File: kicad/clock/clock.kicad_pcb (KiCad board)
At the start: 2 copper layers, 48.9 x 36.2 mm, 22 parts, among them J1 HLT IN, J2 CLK OUT, J3 5V IN, J4 OSC A, J5 OSC B, SW1 SEL, U1 74LS04, U2 74LS08, U3 74LS32, U4 LM555

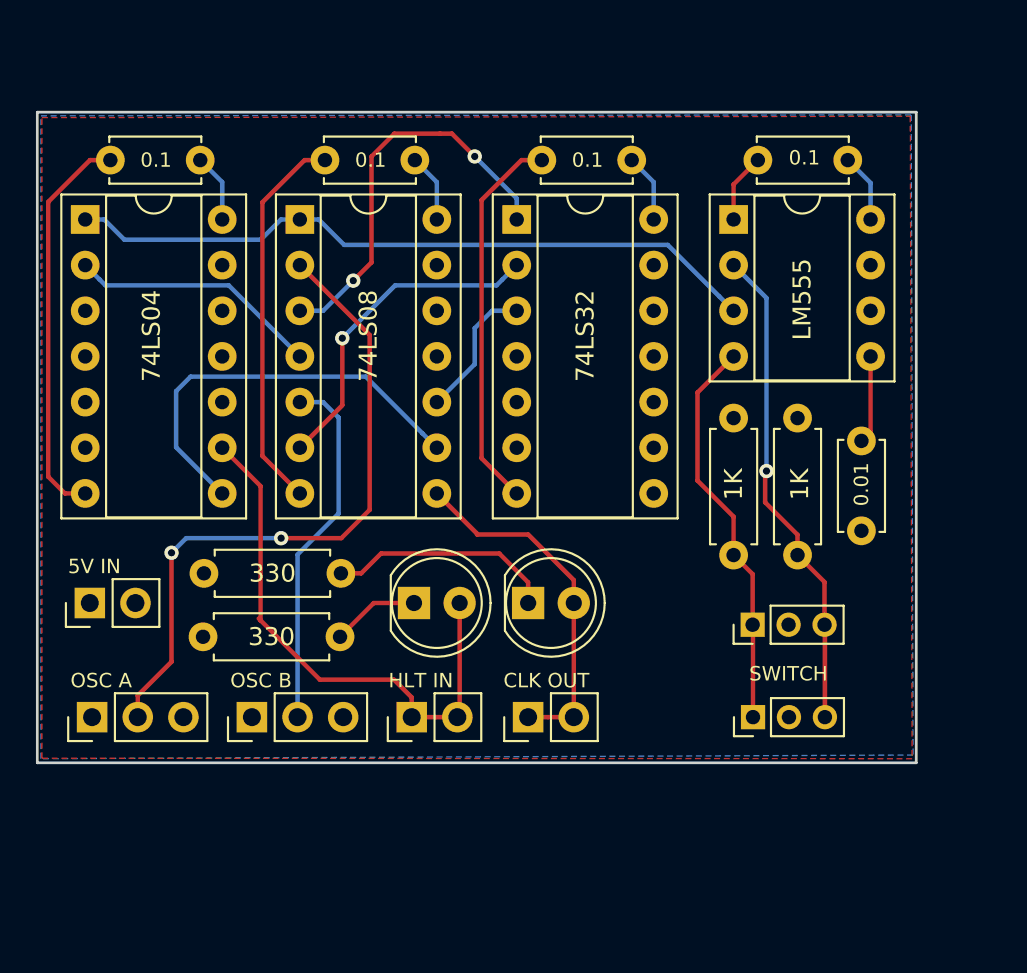
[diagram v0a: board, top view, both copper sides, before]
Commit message: More info on clock, plus gerbers
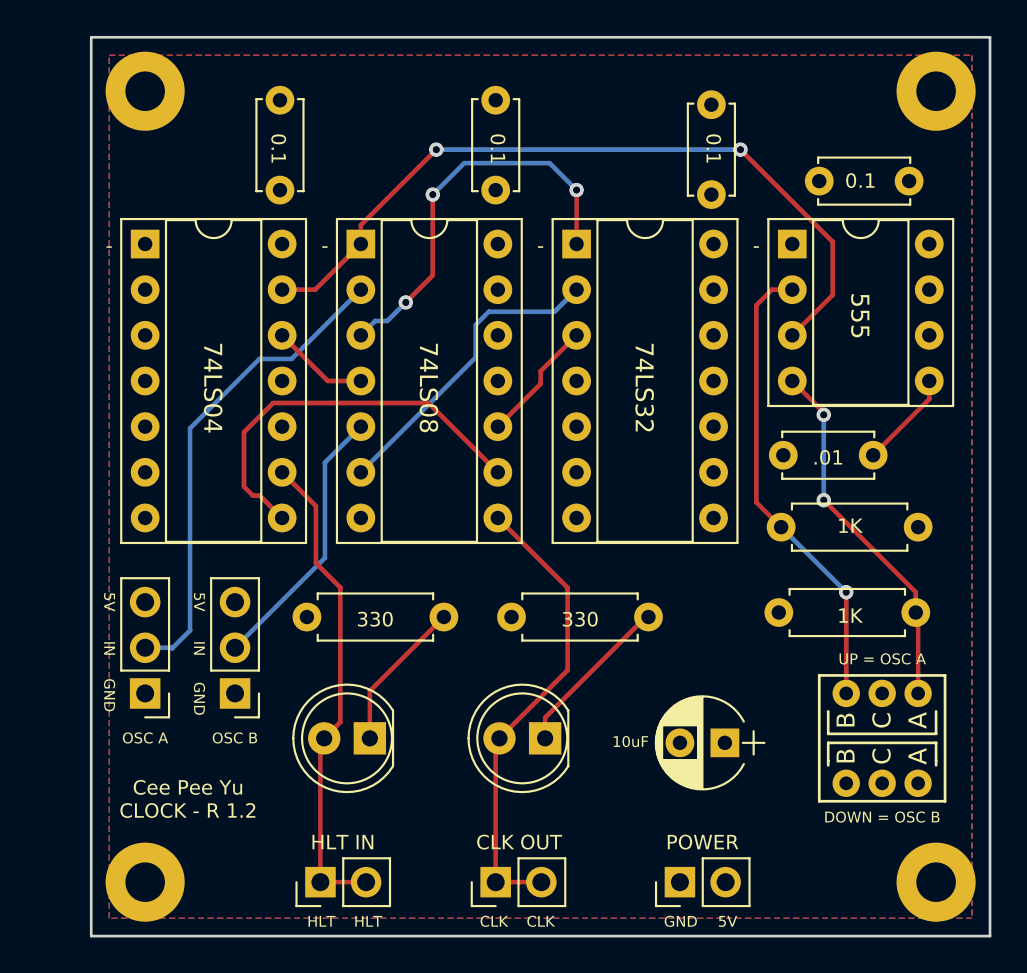
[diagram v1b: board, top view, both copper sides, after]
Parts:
- removed SWITCH: SEL, Socket_Strips:Socket_Strip_Straight_1x03_Pitch2.00mm
- added C6: 0.1uF, Capacitors_THT:C_Disc_D5.0mm_W2.5mm_P5.00mm, F.Cu at (164.5, 54.8)
- added REF**: MountingHole_2.2mm_M2_Pad, Mounting_Holes:MountingHole_2.2mm_M2_Pad, F.Cu at (177.0, 93.0)
- added REF**: MountingHole_2.2mm_M2_Pad, Mounting_Holes:MountingHole_2.2mm_M2_Pad, F.Cu at (133.0, 93.0)
- added REF**: MountingHole_2.2mm_M2_Pad, Mounting_Holes:MountingHole_2.2mm_M2_Pad, F.Cu at (177.0, 49.0)
- added REF**: MountingHole_2.2mm_M2_Pad, Mounting_Holes:MountingHole_2.2mm_M2_Pad, F.Cu at (133.0, 49.0)
- C1, C2, C3: value 0.1 -> 0.1uF
- C4: value 0.01 -> 0.01uF
- C5: value 0.1 -> 10uF; footprint Capacitors_THT:C_Disc_D5.0mm_W2.5mm_P5.00mm -> Capacitors_THT:CP_Radial_D5.0mm_P2.50mm
- J3: value 5V IN -> 5v IN
- SW1: value SEL -> SEL SW; footprint Socket_Strips:Socket_Strip_Straight_1x03_Pitch2.00mm -> Custom_Parts:SW_DPDT_L7mm_P2mm
- moved J3 36.3 mm to (162.8, 93.0)
- moved C5 33.1 mm to (165.2, 85.2)
- moved R2 17.3 mm to (161.0, 78.2)
- moved C3 15.5 mm to (170.5, 54.0)
- moved R4 11.1 mm to (168.2, 78.0), turned to 0 degrees
- moved J1 10.5 mm to (142.8, 93.0)
- moved C2 10.1 mm to (152.5, 49.5), turned to 270 degrees
- moved C1 10.0 mm to (140.5, 49.5), turned to 270 degrees
- moved J2 9.36 mm to (152.5, 93.0)
- moved R3 9.05 mm to (176.0, 73.2), turned to 180 degrees
- moved D1 7.92 mm to (145.5, 85.0), turned to 180 degrees
- moved D2 7.59 mm to (155.2, 85.0), turned to 180 degrees
- moved SW1 7.28 mm to (174.0, 85.0), turned to 270 degrees
- moved R1 5.88 mm to (142.0, 78.2)
- moved U2 3.66 mm to (145.0, 57.5)
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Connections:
- U1 pad 1: /SEL -> (no net)
- U1 pad 12: (no net) -> Net-(U1-Pad12)
- U1 pad 13: (no net) -> /SEL
- U1 pad 2: Net-(U1-Pad2) -> (no net)
- U2 pad 4: Net-(U1-Pad2) -> Net-(U1-Pad12)
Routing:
- net GND: track 68.9 -> 0.00 mm
- net VCC: track 15.3 -> 0.00 mm
- net Net-(U1-Pad2): track 14.0 -> 0.00 mm
- net /OSC_A: track 37.2 -> 26.9 mm, vias 2 -> 0
- net /OUT: track 19.8 -> 26.1 mm
- net Net-(U1-Pad12): track 0.00 -> 5.43 mm
- net /OSC_B: track 20.1 -> 15.2 mm
- net /HLT: track 30.9 -> 27.1 mm
- net /SEL: track 39.1 -> 42.7 mm, vias 0 -> 2
- net Net-(D1-Pad1): track 4.89 -> 8.46 mm
- net Net-(D2-Pad1): track 12.7 -> 9.22 mm
- net Net-(R4-Pad2): track 22.2 -> 20.1 mm, vias 0 -> 2
- net Net-(R3-Pad2): track 27.3 -> 26.0 mm
- net Net-(U2-Pad6): track 18.5 -> 17.3 mm, vias 1 -> 0
- net Net-(U1-Pad8): track 23.2 -> 22.3 mm
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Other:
- board size 48.9 x 36.2 mm -> 50 x 50 mm
- net class Default: clearance 0.2 -> 0.3; trace_width 0.25 -> 0.254
- rule trace_clearance: 0.2 -> 0.3
- board text added: "-"
- board text added: ".01"
- board text added: "0.1"
- board text added: "10uF"
- board text added: "1K"
- board text added: "330"
- board text added: "555"
- board text added: "5V"
- board text added: "74LS04"
- board text added: "74LS08"
- board text added: "74LS32"
- board text added: "CLK"
- board text added: "CLK OUT"
- board text added: "Cee Pee Yu CLOCK - R 1.2"
- board text added: "DOWN = OSC B"
- board text added: "GND"
- board text added: "HLT"
- board text added: "HLT IN"
- board text added: "IN"
- board text added: "OSC A"
- board text added: "OSC B"
- board text added: "POWER"
- board text added: "UP = OSC A"
